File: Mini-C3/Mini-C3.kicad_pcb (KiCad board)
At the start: 2 copper layers, 21.2 x 16.4 mm, 25 parts, among them J1 TB_1X2, J10 Sensor1, J2 Sensor1, J4 MotorB, J5 MotorA, J6 Sensor1, J7 Sensor1, J8 Sensor1, J9 Sensor1, SW1 SW_Push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

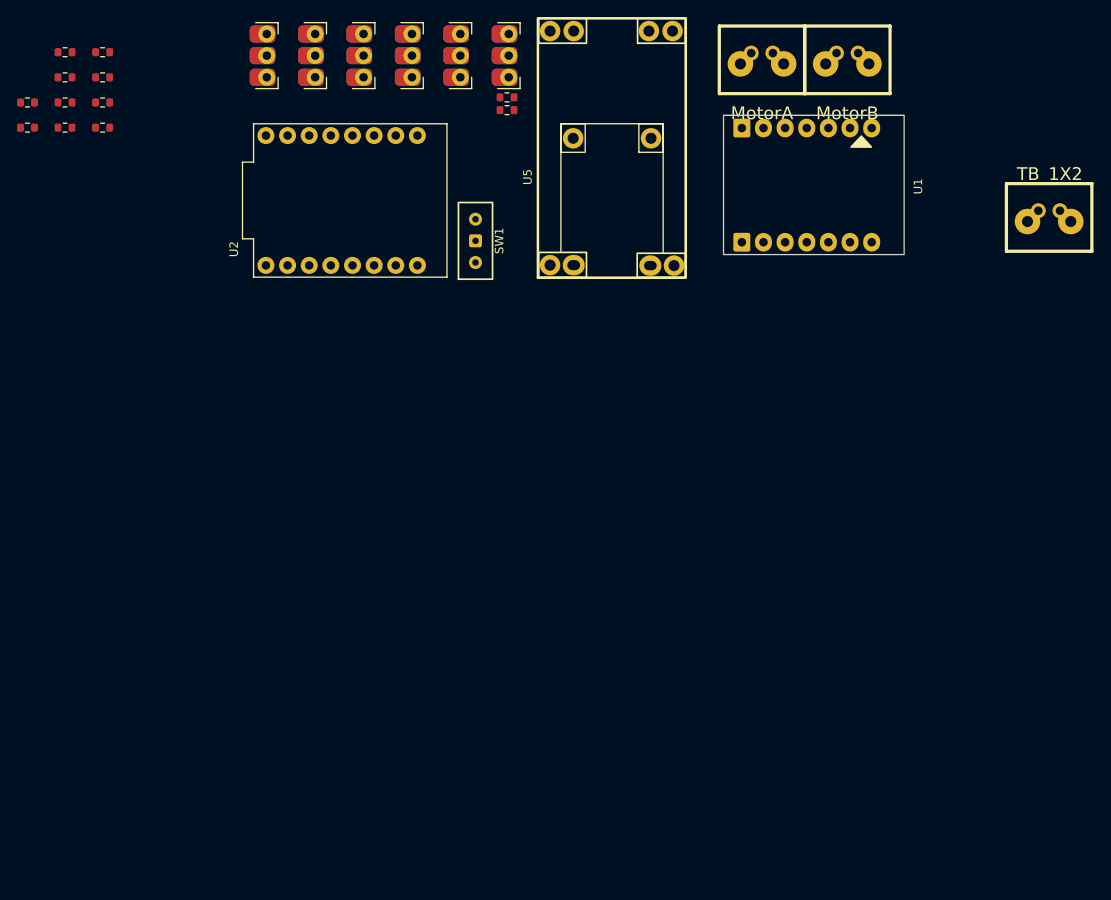
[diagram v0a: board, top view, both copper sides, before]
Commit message: PCB components placement
Improved the placement of the components.
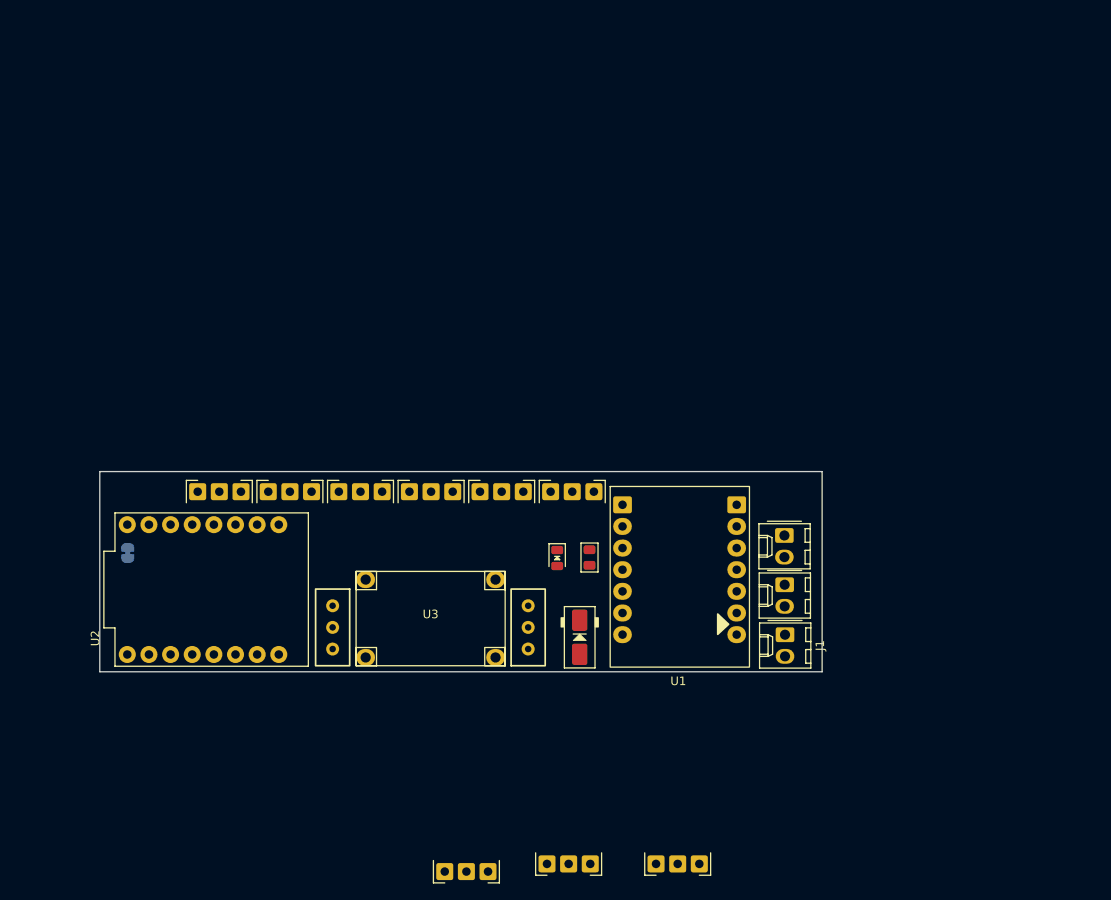
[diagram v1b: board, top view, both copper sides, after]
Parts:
- removed R1, R11, R3, R5, R7, R9: 1.5k, Resistor_SMD:R_0603_1608Metric
- removed R10, R12, R2, R4, R6, R8: 2,7k, Resistor_SMD:R_0603_1608Metric
- removed U5: Mix_Mini360-MP4560, MixLib:Mix_Mini360-MP4560
- added D1: M7, PCM_Diode_SMD_Handsoldering_AKL:D_SMA, F.Cu at (164.4, 99.3)
- added D2: LED, MixLib:LED_0805_2012Metric, F.Cu at (161.8, 90.0)
- added J11: Sensor1, MixLib:PinHeader_1x03_P2.54-THT, F.Cu at (175.9, 125.2)
- added J12: Sensor1, MixLib:PinHeader_1x03_P2.54-THT, F.Cu at (151.1, 126.1)
- added J3: Sensor1, MixLib:PinHeader_1x03_P2.54-THT, F.Cu at (163.1, 125.2)
- added JP7: Jumper_2_Small_Open, Jumper:SolderJumper-2_P1.3mm_Bridged_RoundedPad1.0x1.5mm, B.Cu at (111.4, 89.4)
- added R13: 2,7k, PCM_Resistor_SMD_AKL:R_0805_2012Metric, F.Cu at (165.6, 89.9)
- added SW2: Sensors voltage switch, MixLib:SW_Slide-03_P2.54_L9_W4_H7, F.Cu at (135.4, 98.1)
- added U3: Mini360, MixLib:Mini360_step-down, F.Cu at (146.9, 97.1)
- J1, J4, J5: footprint MixLib:Bornera_2_duo -> Connector_Molex:Molex_KK-254_AE-6410-02A_1x02_P2.54mm_Vertical
- J10, J2, J6, J7, J8, J9: footprint MixLib:PinHeader_1x03_P2.54-SMD,THT,2-layers -> MixLib:PinHeader_1x03_P2.54-THT
- moved J4 61.6 mm to (188.5, 93.1), turned to -90 degrees
- moved J10 59.1 mm to (155.3, 82.9), turned to 180 degrees
- moved J1 57.6 mm to (188.5, 99.0), turned to -90 degrees
- moved J5 55.4 mm to (188.5, 87.3), turned to -90 degrees
- moved J9 52.9 mm to (122.1, 82.9), turned to 180 degrees
- moved J2 52.5 mm to (163.6, 82.9), turned to 180 degrees
- moved J8 52.5 mm to (130.4, 82.9), turned to 180 degrees
- moved J7 52.2 mm to (138.7, 82.9), turned to 180 degrees
- moved J6 52.0 mm to (147.0, 82.9), turned to 180 degrees
- moved U2 48.5 mm to (121.2, 93.7)
- moved U1 48.4 mm to (176.1, 92.1), turned to 0 degrees
- moved SW1 45.8 mm to (158.4, 98.1)
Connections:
- J10 pad 1: Net-(J10-Pin_1) -> GND
- J10 pad 2: GND -> /Pin5
- J10 pad 3: +5V -> /Vcc
- J2 pad 1: Net-(J2-Pin_1) -> GND
- J2 pad 2: GND -> /Pin0
- J2 pad 3: +5V -> /Vcc
- J6 pad 1: Net-(J6-Pin_1) -> GND
- J6 pad 2: GND -> /Pin1
- J6 pad 3: +5V -> /Vcc
- J7 pad 1: Net-(J7-Pin_1) -> GND
- J7 pad 2: GND -> /Pin2
- J7 pad 3: +5V -> /Vcc
- J8 pad 1: Net-(J8-Pin_1) -> GND
- J8 pad 2: GND -> /Pin3
- J8 pad 3: +5V -> /Vcc
- J9 pad 1: Net-(J9-Pin_1) -> GND
- J9 pad 2: GND -> /Pin4
- J9 pad 3: +5V -> /Vcc
- SW1 pad 1: /VM -> Net-(D1-K)
- U1 pad 4: /VREF -> +3.3V
- U2 pad 3.3: unconnected-(U2-3V3-Pad3.3) -> +3.3V
- U2 pad 5V: +5V -> Net-(JP7-A)
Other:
- board size 21.2 x 16.4 mm -> 84.8 x 23.5 mm

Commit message: pecebé
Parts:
- removed SW2: Sensors voltage switch, MixLib:SW_Slide-03_P2.54_L9_W4_H7
- added JP1: Sensors voltage jumper, Jumper:SolderJumper-3_P2.0mm_Open_TrianglePad1.0x1.5mm, B.Cu at (134.5, 86.4)
- D2: footprint MixLib:LED_0805_2012Metric -> MixLib:LED_1206_3216Metric
- J1: footprint Connector_Molex:Molex_KK-254_AE-6410-02A_1x02_P2.54mm_Vertical -> MixLib:MyPinHeader-01x02-vertical
- J4, J5: footprint Connector_Molex:Molex_KK-254_AE-6410-02A_1x02_P2.54mm_Vertical -> MixLib:Bornera_2_duo
- moved J1 24.3 mm to (164.3, 100.0)
- moved SW1 23.2 mm to (135.2, 98.3)
- moved D1 12.9 mm to (151.5, 99.1)
- moved R13 11.9 mm to (153.7, 89.4), turned to 0 degrees
- moved J12 11.0 mm to (149.9, 115.2)
- moved J11 10.1 mm to (174.7, 115.2)
- moved J3 10.1 mm to (161.9, 115.2)
- moved J10 9.39 mm to (145.9, 82.8)
- moved J2 9.39 mm to (154.2, 82.8)
- moved J6 9.39 mm to (137.6, 82.8)
- moved J9 9.39 mm to (112.7, 82.8)
- moved J7 9.39 mm to (129.3, 82.8)
- moved J8 9.39 mm to (121.0, 82.8)
- moved D2 8.26 mm to (153.7, 91.5), turned to 0 degrees
- moved U3 4.71 mm to (143.4, 94.0), turned to 90 degrees
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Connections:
- D2 pad 2: +5V -> /Vcc
- J1 pad 1: /VM -> GND
- J1 pad 2: GND -> /VM
- SW1 pad 1: Net-(D1-K) -> (no net)
- SW1 pad 3: (no net) -> Net-(D1-K)
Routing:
- net +3.3V: track 0.00 -> 19.3 mm

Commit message: la pecebé
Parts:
- moved J12 35.3 mm to (162.5, 82.2)
- moved J11 32.2 mm to (162.5, 85.4)
- moved J3 29.4 mm to (154.2, 86.8), turned to 180 degrees
- moved D2 19.0 mm to (135.0, 88.0)
- moved R13 18.6 mm to (135.3, 91.9)
- moved J1 3.08 mm to (161.2, 99.7)
- moved JP1 2.05 mm to (134.5, 88.4)
- moved J2 0.77 mm to (154.2, 83.6)
- moved J10 0.77 mm to (145.9, 83.6)
- moved J6 0.77 mm to (137.6, 83.6)
- moved J7 0.77 mm to (129.3, 83.6)
- moved J8 0.77 mm to (121.0, 83.6)
- moved J9 0.77 mm to (112.7, 83.6)
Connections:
- J10 pad 1: GND -> /Pin5
- J10 pad 2: /Pin5 -> GND
- J11 pad 1: GND -> /Pin7
- J11 pad 2: /Pin7 -> GND
- J12 pad 1: GND -> /Pin8
- J12 pad 2: /Pin8 -> GND
- J2 pad 1: GND -> /Pin0
- J2 pad 2: /Pin0 -> GND
- J3 pad 1: GND -> /Pin6
- J3 pad 2: /Pin6 -> GND
- J6 pad 2: /Pin1 -> unconnected-(J6-Pin_2-Pad2)
- J7 pad 1: GND -> /Pin2
- J7 pad 2: /Pin2 -> GND
- J8 pad 1: GND -> /Pin3
- J8 pad 2: /Pin3 -> GND
- J9 pad 1: GND -> /Pin4
- J9 pad 2: /Pin4 -> GND
- U2 pad 1: /Pin1 -> GND
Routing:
- net +5V: track 0.00 -> 4.14 mm
- net +3.3V: track 19.3 -> 18.5 mm
- added copper zone on B.Cu, net /Vcc
- added copper zone on F.Cu, net /Vcc
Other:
- board text added: "- CAUTION -"
- board text added: "3.3v"
- board text added: "5v"
- board text added: "Select only one (3.3V / 5V)at a time, otherwise, you will fry the board."

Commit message: PCB almost there
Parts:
- added R1: 100, Resistor_SMD:R_0805_2012Metric, F.Cu at (158.4, 96.4)
- added R2: 100, Resistor_SMD:R_0805_2012Metric, F.Cu at (154.8, 96.4)
- added SW2: SW_Push, Button_Switch_SMD:SW_Tactile_SPST_NO_Straight_CK_PTS636Sx25SMTRLFS, F.Cu at (163.8, 92.5)
- added SW3: SW_DIP_x02, Button_Switch_SMD:SW_DIP_SPSTx02_Slide_6.7x6.64mm_W8.61mm_P2.54mm_LowProfile, F.Cu at (155.1, 91.7)
- D2: footprint MixLib:LED_1206_3216Metric -> MixLib:LED_0805_2012Metric
- JP7: footprint Jumper:SolderJumper-2_P1.3mm_Bridged_RoundedPad1.0x1.5mm -> Jumper:SolderJumper-2_P1.3mm_Open_RoundedPad1.0x1.5mm
- R13: footprint PCM_Resistor_SMD_AKL:R_0805_2012Metric -> Resistor_SMD:R_0805_2012Metric
- moved J11 1.40 mm to (162.5, 86.8), turned to 180 degrees
- moved U1 1.40 mm to (175.3, 91.8)
- moved J12 1.39 mm to (162.5, 83.6), turned to 180 degrees
- moved J5 1.13 mm to (187.7, 86.1)
- moved J4 1.02 mm to (187.7, 96.5)
- moved J1 0.94 mm to (160.4, 100.2)
- moved D1 0.54 mm to (151.0, 99.2), turned to 90 degrees
- moved U3 0.30 mm to (143.1, 94.1)
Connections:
- J10 pad 1: /Pin5 -> GND
- J10 pad 2: GND -> /Pin0
- J11 pad 1: /Pin7 -> GND
- J11 pad 2: GND -> /Pin7
- J12 pad 1: /Pin8 -> GND
- J12 pad 2: GND -> /Pin8
- J2 pad 1: /Pin0 -> GND
- J2 pad 2: GND -> /Pin5
- J3 pad 1: /Pin6 -> GND
- J3 pad 2: GND -> /Pin6
- J6 pad 2: unconnected-(J6-Pin_2-Pad2) -> /Pin1
- J7 pad 1: /Pin2 -> GND
- J7 pad 2: GND -> /Pin2
- J8 pad 1: /Pin3 -> GND
- J8 pad 2: GND -> /Pin3
- J9 pad 1: /Pin4 -> GND
- J9 pad 2: GND -> /Pin4
- SW1 pad 1: (no net) -> Net-(U3-IN)
- SW1 pad 2: Net-(U3-IN) -> Net-(D1-K)
- SW1 pad 3: Net-(D1-K) -> (no net)
- U2 pad 1: GND -> /Pin1
- U2 pad 10: /IN_A2 -> /IN_B1
- U2 pad 20: /IN_B1 -> /IN_A2
- U2 pad 21: /IN_B2 -> /IN_A1
- U2 pad 9: /IN_A1 -> /IN_B2
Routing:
- net /Vcc: track 0.00 -> 76.3 mm, vias 0 -> 1
- net /IN_B1: track 0.00 -> 50.0 mm
- net /IN_A2: track 0.00 -> 45.4 mm
- net /IN_A1: track 0.00 -> 41.8 mm
- net +5V: track 4.14 -> 35.2 mm
- net /Pin0: track 0.00 -> 18.1 mm
- net /Pin8: track 0.00 -> 17.3 mm
- net Net-(D1-K): track 0.00 -> 17.1 mm
- net /VM: track 0.00 -> 17.0 mm, vias 0 -> 11
- net /Pin1: track 0.00 -> 12.4 mm
- net Net-(R2-Pad2): track 0.00 -> 8.86 mm
- net /Pin4: track 0.00 -> 7.47 mm
- net /Pin6: track 0.00 -> 6.83 mm
- net /Pin2: track 0.00 -> 6.64 mm
- net Net-(R1-Pad1): track 0.00 -> 4.45 mm
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- added copper zone on B.Cu, net /OUT_A1
- added copper zone on F.Cu, net /OUT_A1
- added copper zone on B.Cu, net /OUT_A2
- added copper zone on F.Cu, net /OUT_A2
- added copper zone on B.Cu, net /OUT_B1
- added copper zone on F.Cu, net /OUT_B1
- added copper zone on B.Cu, net /OUT_B2
- added copper zone on F.Cu, net /OUT_B2
- added copper zone on B.Cu, net /VM
- added copper zone on F.Cu, net /VM
- added copper zone on B.Cu, net GND
- added copper zone on F.Cu, net GND
- removed copper zone on B.Cu, net /Vcc
- removed copper zone on F.Cu, net /Vcc
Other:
- board size 84.8 x 23.5 mm -> 84.1 x 23.3 mm
- board text added: "+"
- board text added: "-"
- board text added: "Battery"

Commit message: Repositioned & added footprints
Honestly there's so much that was done that I just can't put it all here, also maybe because I don't remember. You should see the changes for yourself. Who reads these anyway?
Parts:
- added C1: 100, Capacitor_THT:C_Disc_D4.3mm_W1.9mm_P5.00mm, F.Cu at (180.5, 98.5)
- added H1: MountingHole_Pad, MountingHole:MountingHole_2.2mm_M2_DIN965_Pad, F.Cu at (190.1, 82.1)
- added H2: MountingHole_Pad, MountingHole:MountingHole_2.2mm_M2_DIN965_Pad, F.Cu at (190.1, 100.8)
- added H3: MountingHole_Pad, MountingHole:MountingHole_2.2mm_M2_DIN965_Pad, F.Cu at (110.6, 82.1)
- D1: footprint PCM_Diode_SMD_Handsoldering_AKL:D_SMA -> Diode_SMD:D_SMA
- J4, J5: footprint MixLib:Bornera_2_duo -> MixLib:MyPinHeader-01x02
- moved R2 5.00 mm to (158.6, 93.1), turned to 180 degrees
- moved J9 3.91 mm to (116.7, 83.6)
- moved J8 3.76 mm to (124.8, 83.6)
- moved J7 3.61 mm to (133.0, 83.6)
- moved J6 3.46 mm to (141.1, 83.6)
- moved J10 3.31 mm to (149.3, 83.6)
- moved J3 3.17 mm to (157.4, 86.8)
- moved J2 3.16 mm to (157.4, 83.6)
- moved J12 3.01 mm to (165.6, 83.6)
- moved J11 3.01 mm to (165.6, 86.8)
- moved D1 2.87 mm to (153.1, 101.1), turned to 0 degrees
- moved SW3 2.77 mm to (152.9, 93.4), turned to -90 degrees
- moved J1 2.55 mm to (162.9, 100.2)
- moved U1 2.50 mm to (177.8, 91.8)
- moved J4 2.38 mm to (189.3, 94.8)
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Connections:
- J11 pad 2: /Pin7 -> /Pin8
- J12 pad 2: /Pin8 -> /Pin7
- SW2 pad 1: /Pin7 -> /Pin8
- SW3 pad 2: /Pin8 -> /Pin7
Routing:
- net /Pin7: track 3.05 -> 71.0 mm, vias 0 -> 1
- net +3.3V: track 17.3 -> 80.4 mm, vias 0 -> 2
- net /IN_B2: track 0.00 -> 58.5 mm
- net /Pin5: track 0.00 -> 55.8 mm, vias 0 -> 1
- net /Pin6: track 6.83 -> 59.6 mm, vias 0 -> 1
- net /Pin8: track 17.3 -> 58.3 mm
- net /VM: track 17.0 -> 12.9 mm, vias 11 -> 21
- net /IN_A1: track 41.8 -> 45.5 mm
- net /Pin2: track 6.64 -> 10.3 mm
- net /IN_B1: track 50.0 -> 53.6 mm
- net /Pin1: track 12.4 -> 15.9 mm
- net /Pin4: track 7.47 -> 4.08 mm
- net /Pin0: track 18.1 -> 21.5 mm
- net /IN_A2: track 45.4 -> 47.9 mm
- net unconnected-(H3-Pad1): track 0.00 -> 1.81 mm
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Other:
- outline, holes or cut-outs redrawn
- board text added: "Max 4S"
- board text added: "P6"
- board text added: "P7"
- board text added: "Select only one (3.3V / 5V) at a time, otherwise, you will fry the board."
- board text added: "V P0 G"
- board text added: "V P1 G"
- board text added: "V P2 G"
- board text added: "V P3 G"
- board text added: "V P4 G"
- board text added: "V P5 G"
- board text added: "V P6 G"
- board text added: "V P7 G"
- board text added: "V P8 G"
- board text removed: "Select only one (3.3V / 5V)at a time, otherwise, you will fry the board."

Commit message: Pin names
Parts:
- added G***: LOGO, LOGO, B.Cu at (158.8, 94.2)
- moved R1 3.54 mm to (158.1, 91.8), turned to 90 degrees
- moved R2 2.55 mm to (158.1, 95.6), turned to -90 degrees
- moved SW2 0.86 mm to (164.2, 93.4), turned to 180 degrees
- moved SW3 0.40 mm to (152.5, 93.4)
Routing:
- net /Pin8: track 58.3 -> 69.6 mm
- net /Pin7: track 71.0 -> 65.6 mm, vias 1 -> 2
- net Net-(R1-Pad1): track 5.72 -> 2.51 mm
- net /Pin6: track 59.6 -> 56.7 mm
- net GND: vias 25 -> 24
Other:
- board text added: "JRegi"
- board text added: "Mini-C3 v1"
- board text added: "P10"
- board text added: "P20"
- board text added: "P21"
- board text added: "P8"
- board text added: "P9"
